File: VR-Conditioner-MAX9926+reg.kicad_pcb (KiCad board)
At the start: 2 copper layers, 19.7 x 19.7 mm, 22 parts, among them J1 8-pin header, J2 Edge, U1 MAX9926UAEE+, U2 AMS1117CD-5.0

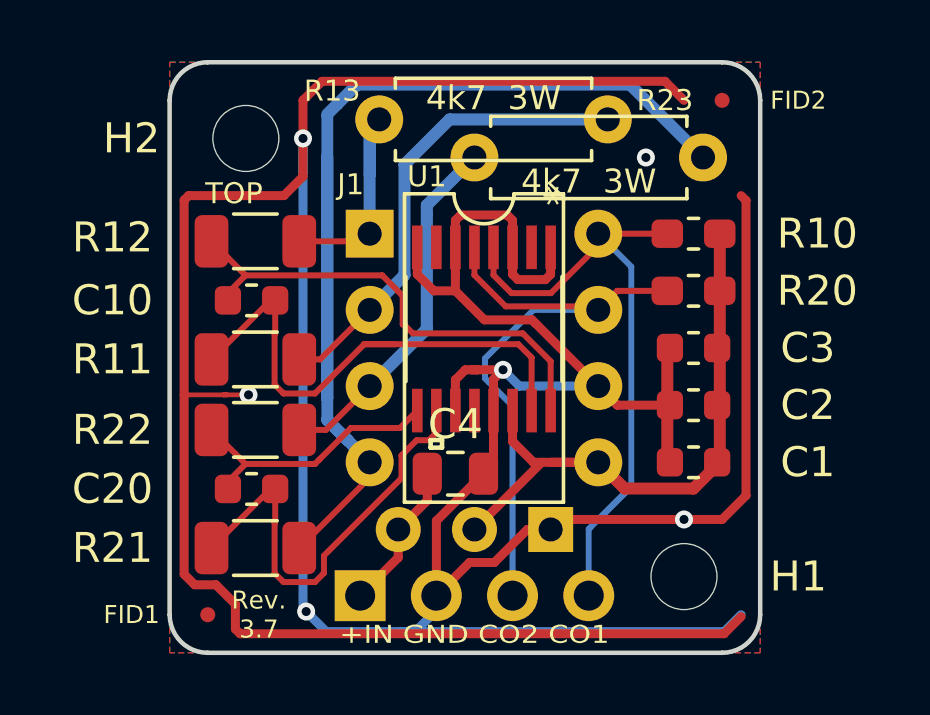
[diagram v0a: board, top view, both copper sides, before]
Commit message: Improve silk screen labeling & ground plane. Added solder pads.
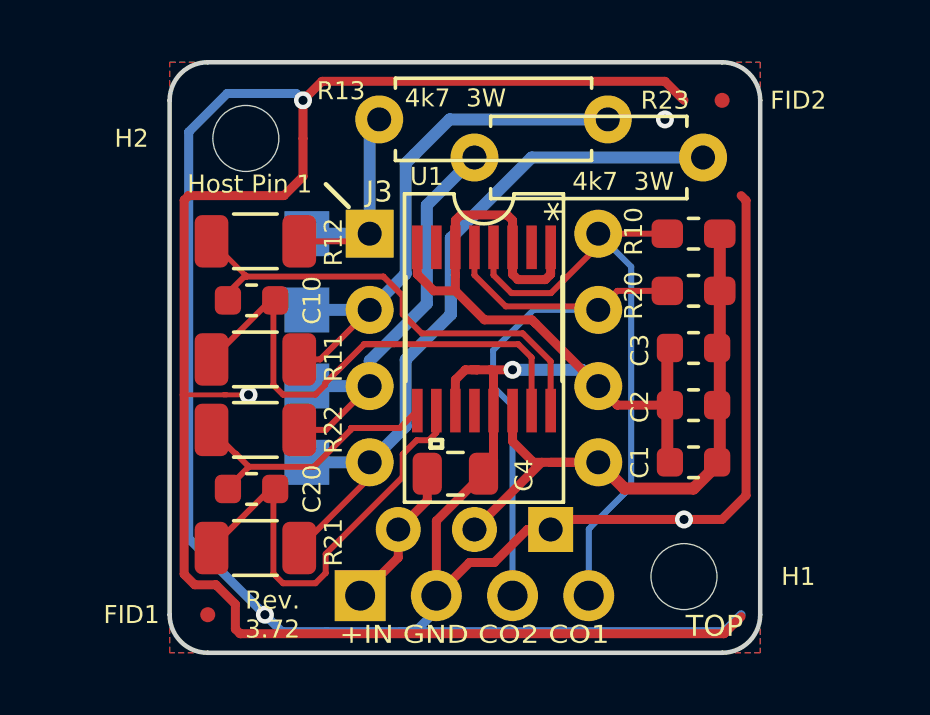
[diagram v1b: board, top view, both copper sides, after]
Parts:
- added TP1: TP, TestPoint:TestPoint_Pad_1.5x1.5mm, B.Cu at (117.0, 102.2)
- added TP2: TP, TestPoint:TestPoint_Pad_1.5x1.5mm, B.Cu at (117.0, 104.8)
- added TP3: TP, TestPoint:TestPoint_Pad_1.5x1.5mm, B.Cu at (117.0, 107.3)
- added TP4: TP, TestPoint:TestPoint_Pad_1.5x1.5mm, B.Cu at (117.0, 109.9)
- renumbered J1 to J3
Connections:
- U1 pad 12: Net-(U1-Pad12) -> unconnected-(U1-Pad12)
- U1 pad 2: Net-(U1-Pad2) -> unconnected-(U1-Pad2)
- U1 pad 7: Net-(U1-Pad7) -> unconnected-(U1-Pad7)
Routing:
- net Net-(J3-Pad4): track 38.5 -> 25.0 mm
- net GND: track 148.7 -> 155.7 mm
- net Net-(J3-Pad2): track 15.8 -> 17.9 mm
- net Net-(J3-Pad3): track 12.0 -> 14.1 mm
- net Net-(C10-Pad1): track 17.0 -> 16.0 mm
- net Net-(J3-Pad1): track 7.60 -> 8.49 mm
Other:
- net class Default removed
- net class Minimum removed
- net class power removed
- board text added: "&MS"
- board text added: "Host Pin 1"
- board text added: "Rev. 3.72"
- board text added: "Speeduino"
- board text added: "compatible"
- board text removed: "Rev. 3.7"
- board text removed: "Speeduino / compatible"
